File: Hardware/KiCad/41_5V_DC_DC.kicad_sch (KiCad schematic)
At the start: 0 parts

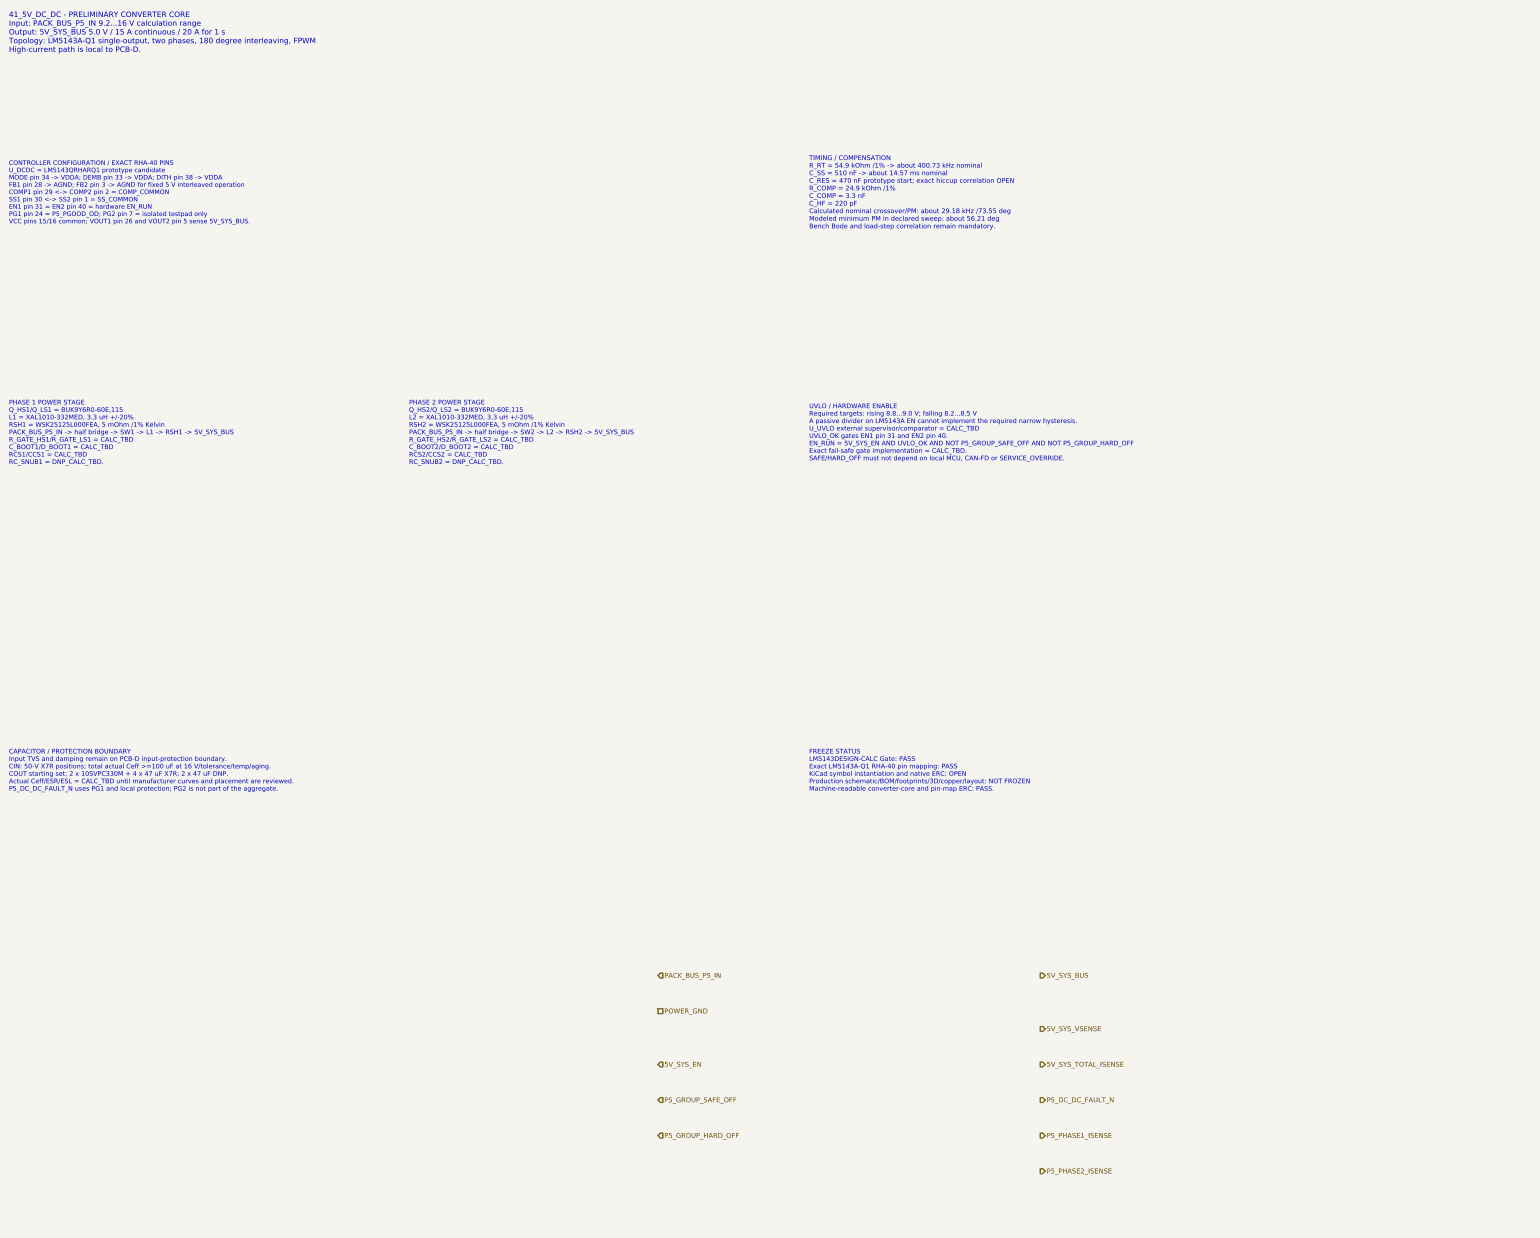
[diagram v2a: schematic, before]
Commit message: hardware: materialize PCB-D KiCad symbol gate
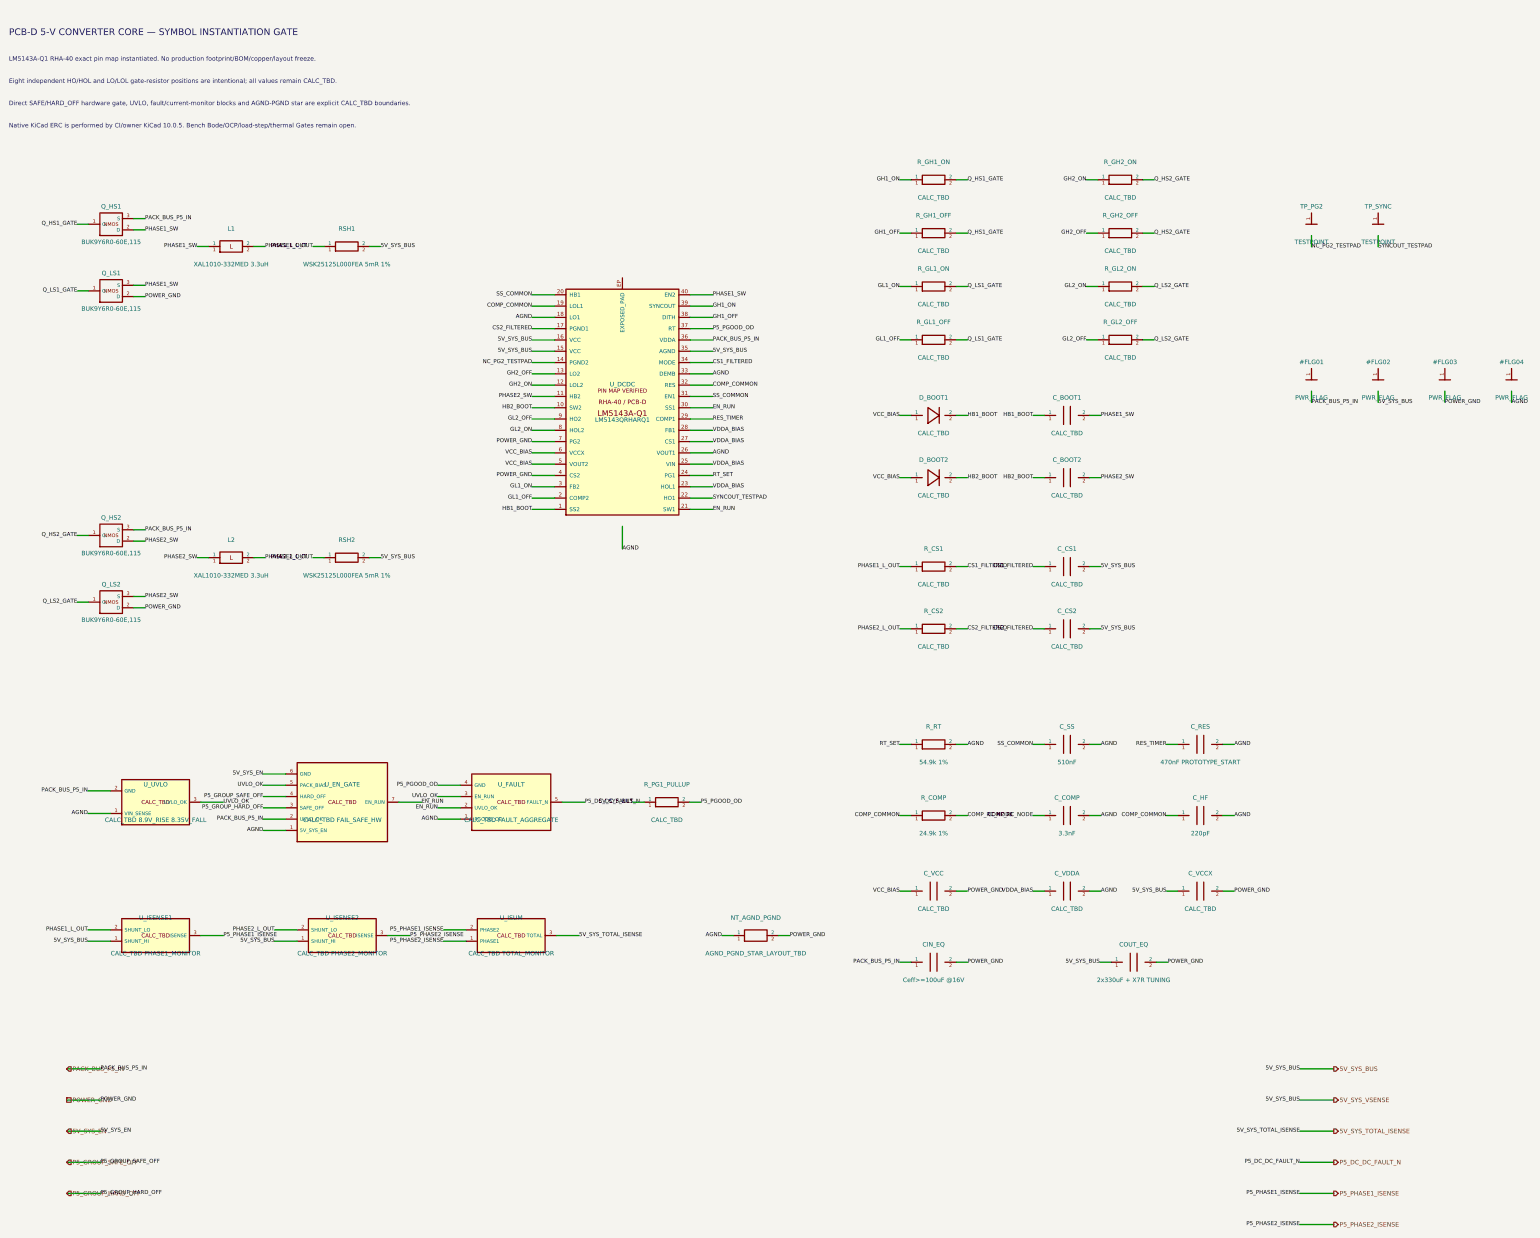
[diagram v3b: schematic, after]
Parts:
- added CIN_EQ: Ceff>=100uF @16V, symbol plataVM:C
- added COUT_EQ: 2x330uF + X7R TUNING, symbol plataVM:C
- added C_BOOT1, C_BOOT2, C_CS1, C_CS2, C_VCC, C_VCCX, C_VDDA: CALC_TBD, symbol plataVM:C
- added C_COMP: 3.3nF, symbol plataVM:C
- added C_HF: 220pF, symbol plataVM:C
- added C_RES: 470nF PROTOTYPE_START, symbol plataVM:C
- added C_SS: 510nF, symbol plataVM:C
- added D_BOOT1, D_BOOT2: CALC_TBD, symbol plataVM:D
- added L1, L2: XAL1010-332MED 3.3uH, symbol plataVM:L
- added NT_AGND_PGND: AGND_PGND_STAR_LAYOUT_TBD, symbol plataVM:NET_TIE_TBD
- added Q_HS1, Q_HS2, Q_LS1, Q_LS2: BUK9Y6R0-60E,115, symbol plataVM:NMOS_POWER
- added RSH1, RSH2: WSK25125L000FEA 5mR 1%, symbol plataVM:R
- added R_COMP: 24.9k 1%, symbol plataVM:R
- added R_CS1, R_CS2, R_GH1_OFF, R_GH1_ON, R_GH2_OFF, R_GH2_ON, R_GL1_OFF, R_GL1_ON, R_GL2_OFF, R_GL2_ON, R_PG1_PULLUP: CALC_TBD, symbol plataVM:R
- added R_RT: 54.9k 1%, symbol plataVM:R
- added TP_PG2, TP_SYNC: TESTPOINT, symbol plataVM:TESTPOINT
- added U_DCDC: LM5143QRHARQ1, symbol plataVM:LM5143A_Q1_RHA40
- added U_EN_GATE: CALC_TBD FAIL_SAFE_HW, symbol plataVM:HW_ENABLE_GATE_TBD
- added U_FAULT: CALC_TBD FAULT_AGGREGATE, symbol plataVM:FAULT_EXPORT_TBD
- added U_ISENSE1: CALC_TBD PHASE1_MONITOR, symbol plataVM:ISENSE_EXPORT_TBD
- added U_ISENSE2: CALC_TBD PHASE2_MONITOR, symbol plataVM:ISENSE_EXPORT_TBD
- added U_ISUM: CALC_TBD TOTAL_MONITOR, symbol plataVM:ISENSE_SUM_TBD
- added U_UVLO: CALC_TBD 8.9V_RISE 8.35V_FALL, symbol plataVM:UVLO_SUPERVISOR_TBD
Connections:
- net 5V_SYS_BUS: now also COUT_EQ.1, C_CS1.2, C_CS2.2, C_VCCX.1, RSH1.2, RSH2.2, R_PG1_PULLUP.1, U_DCDC.15 (VCC), U_DCDC.16 (VCC), U_DCDC.35 (AGND), U_ISENSE1.1 (SHUNT_HI), U_ISENSE2.1 (SHUNT_HI)
- net 5V_SYS_EN: now also U_EN_GATE.6 (GND)
- net 5V_SYS_TOTAL_ISENSE: now also U_ISUM.3 (TOTAL)
- net P5_DC_DC_FAULT_N: now also U_FAULT.5 (FAULT_N)
- net P5_GROUP_HARD_OFF: now also U_EN_GATE.3 (SAFE_OFF)
- net P5_GROUP_SAFE_OFF: now also U_EN_GATE.4 (HARD_OFF)
- net P5_PHASE1_ISENSE: now also U_ISENSE1.3 (ISENSE), U_ISUM.2 (PHASE2)
- net P5_PHASE2_ISENSE: now also U_ISENSE2.3 (ISENSE), U_ISUM.1 (PHASE1)
- net PACK_BUS_P5_IN: now also CIN_EQ.1, Q_HS1.3 (S), Q_HS2.3 (S), U_DCDC.36 (VDDA), U_EN_GATE.2 (UVLO_OK), U_UVLO.2 (GND)
- net POWER_GND: now also CIN_EQ.2, COUT_EQ.2, C_VCC.2, C_VCCX.2, NT_AGND_PGND.2, Q_LS1.2 (D), Q_LS2.2 (D), U_DCDC.4 (CS2), U_DCDC.7 (PG2)
- new net AGND: C_COMP.2, C_HF.2, C_RES.2, C_SS.2, C_VDDA.2, NT_AGND_PGND.1, R_RT.2, U_DCDC.18 (LO1), U_DCDC.26 (VOUT1), U_DCDC.33 (DEMB), U_EN_GATE.1 (5V_SYS_EN), U_FAULT.1 (PGOOD_OD), U_UVLO.1 (VIN_SENSE)
- new net COMP_COMMON: C_HF.1, R_COMP.1, U_DCDC.19 (LOL1), U_DCDC.32 (RES)
- new net COMP_RC_NODE: C_COMP.1, R_COMP.2
- new net CS1_FILTERED: C_CS1.1, R_CS1.2, U_DCDC.34 (MODE)
- new net CS2_FILTERED: C_CS2.1, R_CS2.2, U_DCDC.17 (PGND1)
- new net EN_RUN: U_DCDC.21 (SW1), U_DCDC.30 (SS1), U_EN_GATE.7 (EN_RUN), U_FAULT.2 (UVLO_OK)
- new net GH1_OFF: R_GH1_OFF.1, U_DCDC.38 (DITH)
- new net GH1_ON: R_GH1_ON.1, U_DCDC.39 (SYNCOUT)
- new net GH2_OFF: R_GH2_OFF.1, U_DCDC.13 (LO2)
- new net GH2_ON: R_GH2_ON.1, U_DCDC.12 (LOL2)
- new net GL1_OFF: R_GL1_OFF.1, U_DCDC.2 (COMP2)
- new net GL1_ON: R_GL1_ON.1, U_DCDC.3 (FB2)
- new net GL2_OFF: R_GL2_OFF.1, U_DCDC.9 (HO2)
- new net GL2_ON: R_GL2_ON.1, U_DCDC.8 (HOL2)
- new net HB1_BOOT: C_BOOT1.1, D_BOOT1.2, U_DCDC.1 (SS2)
- new net HB2_BOOT: C_BOOT2.1, D_BOOT2.2, U_DCDC.10 (SW2)
- new net NC_PG2_TESTPAD: U_DCDC.14 (PGND2)
- new net P5_PGOOD_OD: R_PG1_PULLUP.2, U_DCDC.37 (RT), U_FAULT.4 (GND)
- new net PHASE1_L_OUT: L1.2, RSH1.1, R_CS1.1, U_ISENSE1.2 (SHUNT_LO)
- new net PHASE1_SW: C_BOOT1.2, L1.1, Q_HS1.2 (D), Q_LS1.3 (S), U_DCDC.40 (EN2)
- new net PHASE2_L_OUT: L2.2, RSH2.1, R_CS2.1, U_ISENSE2.2 (SHUNT_LO)
- new net PHASE2_SW: C_BOOT2.2, L2.1, Q_HS2.2 (D), Q_LS2.3 (S), U_DCDC.11 (HB2)
- new net Q_HS1_GATE: Q_HS1.1 (G), R_GH1_OFF.2, R_GH1_ON.2
- new net Q_HS2_GATE: Q_HS2.1 (G), R_GH2_OFF.2, R_GH2_ON.2
- new net Q_LS1_GATE: Q_LS1.1 (G), R_GL1_OFF.2, R_GL1_ON.2
- new net Q_LS2_GATE: Q_LS2.1 (G), R_GL2_OFF.2, R_GL2_ON.2
- new net RES_TIMER: C_RES.1, U_DCDC.29 (COMP1)
- new net RT_SET: R_RT.1, U_DCDC.24 (PG1)
- new net SS_COMMON: C_SS.1, U_DCDC.20 (HB1), U_DCDC.31 (EN1)
- new net SYNCOUT_TESTPAD: U_DCDC.22 (HO1)
- new net UVLO_OK: U_EN_GATE.5 (PACK_BIAS), U_FAULT.3 (EN_RUN), U_UVLO.3 (UVLO_OK)
- new net VCC_BIAS: C_VCC.1, D_BOOT1.1, D_BOOT2.1, U_DCDC.5 (VOUT2), U_DCDC.6 (VCCX)
- new net VDDA_BIAS: C_VDDA.1, U_DCDC.23 (HOL1), U_DCDC.25 (VIN), U_DCDC.27 (CS1), U_DCDC.28 (FB1)
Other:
- note added: "Direct SAFE/HARD_OFF hardware gate, UVLO, fault/current-monitor blocks and AGND-PGND star are explicit CALC_TBD boundaries."
- note added: "Eight independent HO/HOL and LO/LOL gate-resistor positions are intentional; all values remain CALC_TBD."
- note added: "LM5143A-Q1 RHA-40 exact pin map instantiated. No production footprint/BOM/copper/layout freeze."
- note added: "Native KiCad ERC is performed by CI/owner KiCad 10.0.5. Bench Bode/OCP/load-step/thermal Gates remain open."
- note added: "PCB-D 5-V CONVERTER CORE — SYMBOL INSTANTIATION GATE"
- note removed: "41_5V_DC_DC - PRELIMINARY CONVERTER CORE Input: PACK_BUS_P5_IN 9.2...16 V calculation range Output: 5V_SYS_BUS 5.0 V / 15 A continuous / 20 A for 1 s Topology: LM5143A-Q1 single-output, two phases, 180 degree interleaving, FPWM High-current path is local to PCB-D."
- note removed: "CAPACITOR / PROTECTION BOUNDARY Input TVS and damping remain on PCB-D input-protection boundary. CIN: 50-V X7R positions; total actual Ceff >=100 uF at 16 V/tolerance/temp/aging. COUT starting set: 2 x 10SVPC330M + 4 x 47 uF X7R; 2 x 47 uF DNP. Actual Ceff/ESR/ESL = CALC_TBD until manufacturer curves and placement are reviewed. P5_DC_DC_FAULT_N uses PG1 and local protection; PG2 is not part of th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"
- note removed: "CONTROLLER CONFIGURATION / EXACT RHA-40 PINS U_DCDC = LM5143QRHARQ1 prototype candidate MODE pin 34 -> VDDA; DEMB pin 33 -> VDDA; DITH pin 38 -> VDDA FB1 pin 28 -> AGND; FB2 pin 3 -> AGND for fixed 5 V interleaved operation COMP1 pin 29 <-> COMP2 pin 2 = COMP_COMMON SS1 pin 30 <-> SS2 pin 1 = SS_COMMON EN1 pin 31 = EN2 pin 40 = hardware EN_RUN PG1 pin 24 = P5_PGOOD_OD; PG2 pin 7 = isolated testpa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"
- note removed: "FREEZE STATUS LM5143DESIGN-CALC Gate: PASS Exact LM5143A-Q1 RHA-40 pin mapping: PASS KiCad symbol instantiation and native ERC: OPEN Production schematic/BOM/footprints/3D/copper/layout: NOT FROZEN Machine-readable converter-core and pin-map ERC: PASS."
- note removed: "PHASE 1 POWER STAGE Q_HS1/Q_LS1 = BUK9Y6R0-60E,115 L1 = XAL1010-332MED, 3.3 uH +/-20% RSH1 = WSK25125L000FEA, 5 mOhm /1% Kelvin PACK_BUS_P5_IN -> half bridge -> SW1 -> L1 -> RSH1 -> 5V_SYS_BUS R_GATE_HS1/R_GATE_LS1 = CALC_TBD C_BOOT1/D_BOOT1 = CALC_TBD RCS1/CCS1 = CALC_TBD RC_SNUB1 = DNP_CALC_TBD."
- note removed: "PHASE 2 POWER STAGE Q_HS2/Q_LS2 = BUK9Y6R0-60E,115 L2 = XAL1010-332MED, 3.3 uH +/-20% RSH2 = WSK25125L000FEA, 5 mOhm /1% Kelvin PACK_BUS_P5_IN -> half bridge -> SW2 -> L2 -> RSH2 -> 5V_SYS_BUS R_GATE_HS2/R_GATE_LS2 = CALC_TBD C_BOOT2/D_BOOT2 = CALC_TBD RCS2/CCS2 = CALC_TBD RC_SNUB2 = DNP_CALC_TBD."
- note removed: "TIMING / COMPENSATION R_RT = 54.9 kOhm /1% -> about 400.73 kHz nominal C_SS = 510 nF -> about 14.57 ms nominal C_RES = 470 nF prototype start; exact hiccup correlation OPEN R_COMP = 24.9 kOhm /1% C_COMP = 3.3 nF C_HF = 220 pF Calculated nominal crossover/PM: about 29.18 kHz /73.55 deg Modeled minimum PM in declared sweep: about 56.21 deg Bench Bode and load-step correlation remain mandatory."
- note removed: "UVLO / HARDWARE ENABLE Required targets: rising 8.8...9.0 V; falling 8.2...8.5 V A passive divider on LM5143A EN cannot implement the required narrow hysteresis. U_UVLO external supervisor/comparator = CALC_TBD UVLO_OK gates EN1 pin 31 and EN2 pin 40. EN_RUN = 5V_SYS_EN AND UVLO_OK AND NOT P5_GROUP_SAFE_OFF AND NOT P5_GROUP_HARD_OFF Exact fail-safe gate implementation = CALC_TBD. SAFE/HARD_OFF mu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"
- title: 41_5V_DC_DC - PCB-D converter core V1.9 -> 41_5V_DC_DC - PCB-D converter core exact-symbol Gate V1.9
